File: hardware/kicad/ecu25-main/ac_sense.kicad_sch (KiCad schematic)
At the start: 80 parts, among them J5 Screw_Terminal_GEN, J6 Screw_Terminal_MAINS, J7 Screw_Terminal_CT, U10 MCP6002, U8 MCP6002, U9 MCP6002

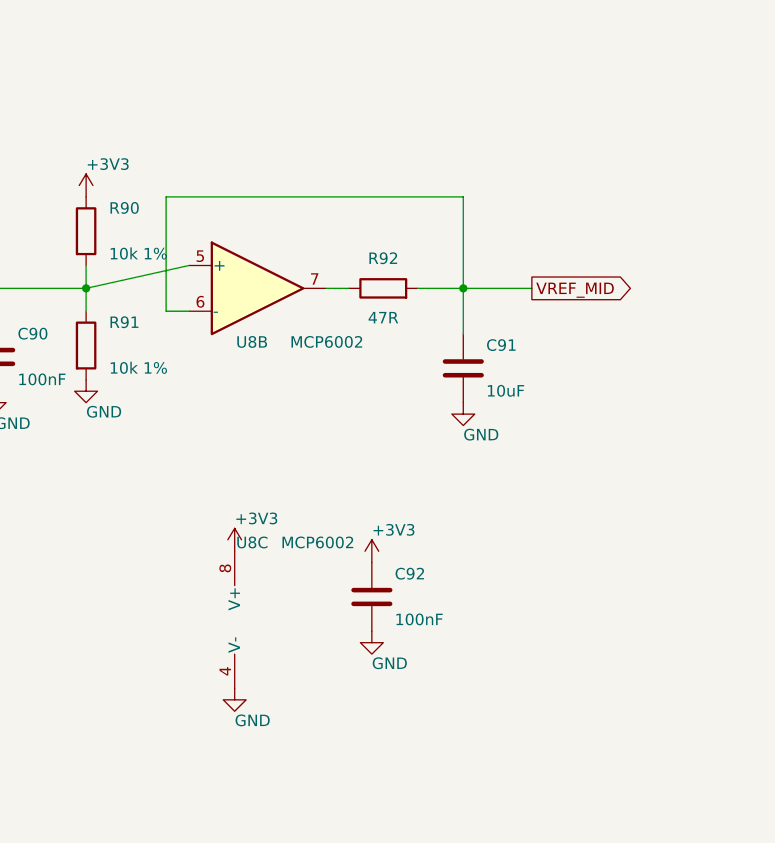
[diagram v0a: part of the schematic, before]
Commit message: Fix SME review findings: 3 critical, 6 major schematic faults
Critical:
- RON pin no longer shorted to GND (R4 moved off C3's column)
- LM2903 MPU comparator +/- inputs unmerged (separate route columns)
- Supercap charge diode D70 un-reversed (anode to +3V3)

Major:
- Buck UVLO divider restored (stray EN stub ended on C3 column = EN
  tied to +24V; stub removed)
- RS485 fail-safe bias polarity corrected (pull-up A, pull-down B)
- U8 spare op-amp unit placed and tied off (was floating on VREF die)
- Heartbeat LED DS1 un-reversed
- VREF_MID buffer dual feedback added (R93 DC path + C93 AC path)
- D80 value SMBJ33A -> SMBJ33CA (bidirectional, matches symbol)

Added netlist-level sweep check (shorted 2-pin devices, rail
membership) since the geometric tracer is blind to shorts closed
through power symbols across wire islands. Sweep: CLEAN, 0 issues.
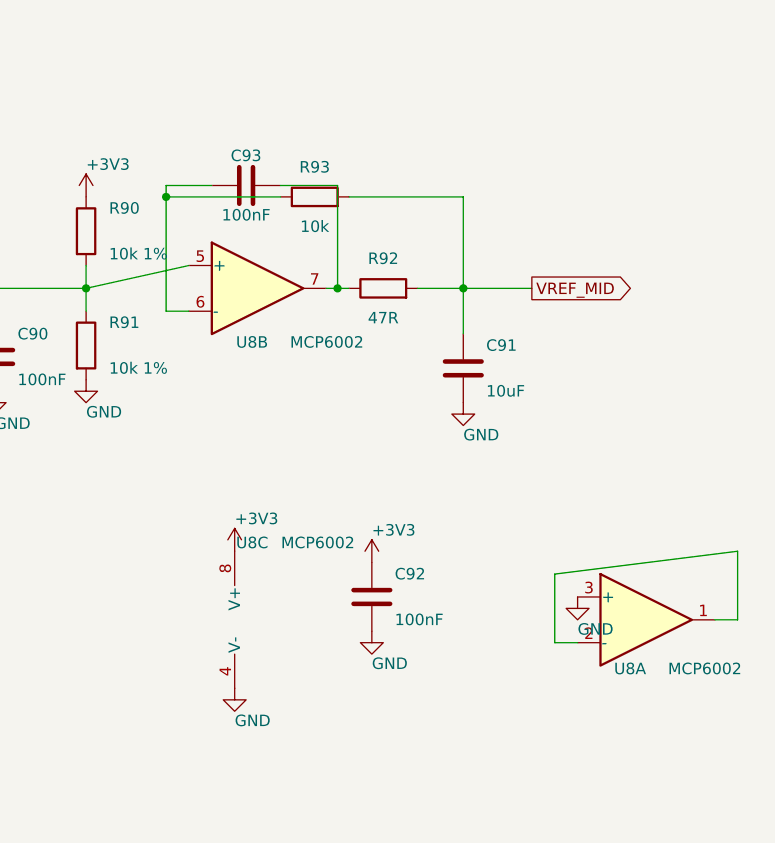
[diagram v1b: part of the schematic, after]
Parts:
- added C93: 100nF, symbol Device:C
- added R93: 10k, symbol Device:R
- added unit 1 of U8
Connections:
- net GND: now also U8.3 (+)
- net VREF_MID: now also R93.2; no longer U8.6 (-)
- net at R92.1, U8.7: now also C93.2
- new net: C93.1, R93.1, U8.6 (-)
- new net: U8.1, U8.2 (-)

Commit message: Assign footprints to all 299 components in schematic generator
- By-ref exceptions + per-symbol defaults + value rules (wattage/voltage classes)
- Field connectors: MKDS-3 for battery/AC/CT/relay terminals, MKDS-1,5 for signal
- Q1 reverse-protection FET: Q_PMOS_GSD -> Q_PMOS_GDS + TO-252-2 (DPAK pad
  numbering 1=G 2=D 3=S; GSD variant would swap D/S in the netlist), part
  SQD50P06-15L
- Verified: all footprint files exist in KiCad 7 libs, all symbol pin numbers
  present in footprint pads, netlist sweep still clean
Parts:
- C40, C41, C42, C43, C44, C45, C50, C51, C52, C90, C92, C93, C96, C97: footprint (none) -> Capacitor_SMD:C_0603_1608Metric
- C91: footprint (none) -> Capacitor_SMD:C_0805_2012Metric
- D40, D41, D42, D43, D44, D45: footprint (none) -> Package_TO_SOT_SMD:SOT-23
- D50, D51, D52: footprint (none) -> Diode_SMD:D_SMB
- J5, J6: footprint (none) -> TerminalBlock_Phoenix:TerminalBlock_Phoenix_MKDS-3-4-5.08_1x04_P5.08mm_Horizontal
- J7: footprint (none) -> TerminalBlock_Phoenix:TerminalBlock_Phoenix_MKDS-3-6-5.08_1x06_P5.08mm_Horizontal
- R300, R301, R302, R303, R310, R311, R312, R313, R320, R321, R322, R323, R330, R331, R332, R333, R340, R341, R342, R343, R350, R351, R352, R353: footprint (none) -> Resistor_SMD:R_1206_3216Metric
- R304, R305, R314, R315, R324, R325, R334, R335, R344, R345, R354, R355, R51, R52, R53, R56, R57, R58, R64, R65, R66, R90, R91, R92, R93: footprint (none) -> Resistor_SMD:R_0603_1608Metric
- R50, R55, R59: footprint (none) -> Resistor_SMD:R_2512_6332Metric
- U10, U8, U9: footprint (none) -> Package_SO:SOIC-8_3.9x4.9mm_P1.27mm

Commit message: Fix PCB SME review findings: relay pin map, 415V clearances, terminal creepage
CRITICAL: G5LE-1 pin map — lib symbol/footprint has coil on pins 2/5, COM 1,
NO 3, NC 4; generator assumed 1/2 coil + 3/4/5 contacts, netting all six
relays dead (coil open, outputs on NC, volt-free GEN/MAINS contacts tied to
logic GND through the driver FETs). Relay sheet rewired, verified by netlist.

MAJOR fixes, all generator-side:
- Volt-free contactor pairs split off J8 onto new J15; J5/J6/J15 are 8-pole
  5.08mm blocks with only odd poles wired (10.16mm live pitch) + pad remap —
  fully-populated 400V-class blocks don't meet PD2 creepage for 415V L-L /
  unsynchronized-source spacing
- DRU rebuilt: GND no longer swept into the line class (was making the board
  unroutable), 3.0mm line class now includes the J15 contactor nets, per-chain
  1.0mm exemptions so the first 330k doesn't false-trip, netless-pad rule,
  generated-file header
- Copper-pour keepouts under J5/J6, the 330k chains, and the volt-free
  contact corridor K3/K4 -> J15
- CT burden + TVS fixed at J7; buck hot loop (C3/U1/L2/C5/C6) and input chain
  fixed in electrical order; R88 (2.6W) moved to the board edge away from
  precision analog; packer margin 0.4 -> 0.6mm
- F2 PTC now specified 60V (sees the 53V load-dump clamp while tripped)

Docs + diagrams + PDFs synced; verified: no overlaps, nothing outside
outline, odd-pole remap correct on J5/J6/J15, netlist sweep clean
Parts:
- J5, J6: footprint TerminalBlock_Phoenix:TerminalBlock_Phoenix_MKDS-3-4-5.08_1x04_P5.08mm_Horizontal -> TerminalBlock_Phoenix:TerminalBlock_Phoenix_MKDS-3-8-5.08_1x08_P5.08mm_Horizontal

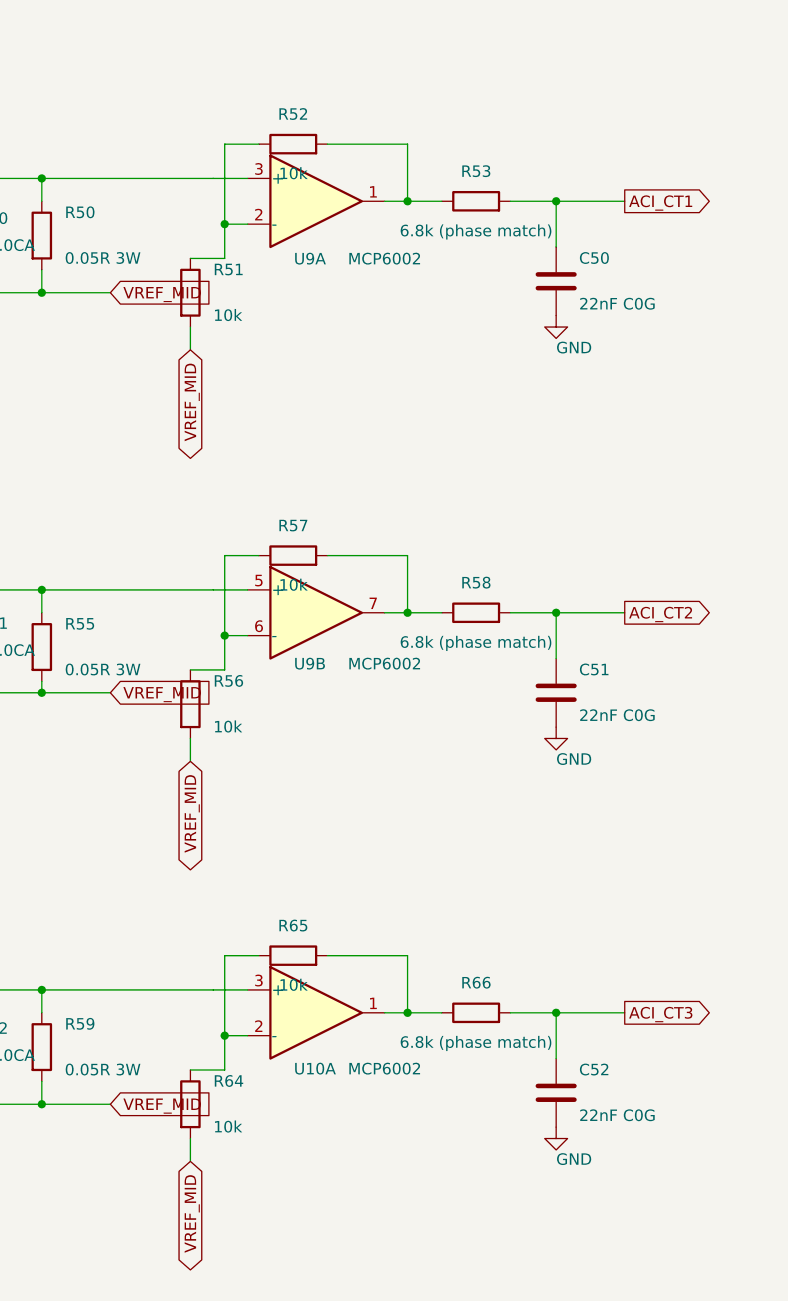
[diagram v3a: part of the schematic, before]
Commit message: Add BOM generator + breadboard prototyping guide; fix parts found by review
New:
- gen_bom.py: builds docs/bom/ecu25-main-bom.{md,csv} from the netlist —
  300 components in 91 order lines, grouped by orderable value + package,
  with part numbers for the actives and a shared-across-sheets section
- docs/bom/breadboard-prototype.md: through-hole translation in eight blocks
  (digital input, relay driver, sender current source, VREF buffer, MPU
  comparator, CT, AC sense, comms), each with an explicit node list, a
  reference-schematic link, and a test that proves that block. Safety rules
  for the 415V sensing (not on a breadboard), CT open-circuit, grounding,
  and supply current limiting

Design corrections the BOM review reached back into:
- F2 was specified as a 60V 1812 PPTC that does not exist (the 0ZCJ0110 is
  8V/1206) -> RXEF110, 72V radial, on Fuse_Bourns_MF-RG900 (1.01mm drill for
  its 0.81mm leads)
- C1 50V -> 63V and C2 50V -> 100V: both sit on +24V, which D1 clamps to ~53V
- CT gain pairs (R51/R52, R56/R57, R64/R65) and the phase-match resistors
  (R53/R58/R66) now carry explicit 1% — 5% pairs would give up to 7% gain
  error on every current and power reading
- G5LE-1-DC24 coil is 1.44k / 400mW / 16.7mA, not 360R / 67mA: a 4x error
  that had propagated through three documents. Every sizing decision was made
  against the larger number, so all of them keep margin
- F2 also gates the four switched outputs, not just the coils — documented

Board:
- Netclasses in .kicad_pro (Battery/Power/Logic/GND/HV_AC/HV_CHAIN) with
  track widths and clearances; +3V3/+5V split into Logic because the
  LQFP-100's own pads are 0.2mm apart and cannot take a wide clearance class
- GND pour fills at the widest non-HV class, with keepouts around every NPTH
  barrel; minimum through-drill 0.2mm to match U1's library thermal vias
- Board now reports zero DRC errors (unrouted ratsnest and silk warnings
  aside), no courtyard overlaps, nothing outside the outline

Also: route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
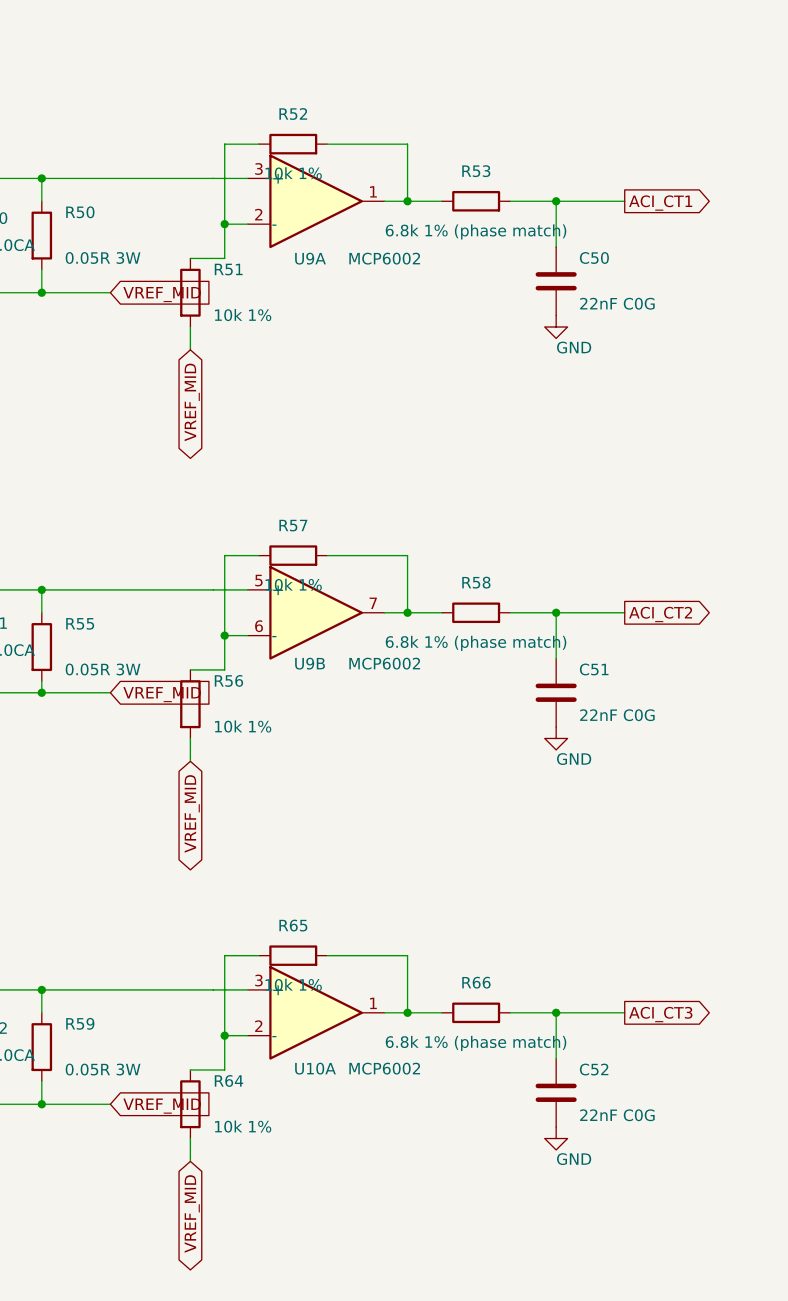
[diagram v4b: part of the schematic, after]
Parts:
- R51, R52, R56, R57, R64, R65: value 10k -> 10k 1%
- R53, R58, R66: value 6.8k (phase match) -> 6.8k 1% (phase match)
